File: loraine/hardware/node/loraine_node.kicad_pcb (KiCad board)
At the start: 2 copper layers, 50.8 x 53.3 mm, 41 parts, among them CON1 BARREL_JACK, IC1 ATTINY2313A-S, P1 POWER_THRU, P2 POWER, P3 SOLDER_PAD, P4 ICSP, P5 OUTPUTS, P6 BUS, P7 BUS_THRU, Q1 BD679, Q2 BD679, Q3 BD679, Q4 BD679, Q5 BD679, Q6 BD679, Q7 BD679, Q8 BD679, U1 UA7805CKCT, U2 SN65176BD, U3 TL4242, U4 TL4242, U5 TL4242, X1 16MHz

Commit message: Split boards
Removed LEDs and TL4242s and sense resistors from main node board and added 3x SIL3 connectors
Added 2nd board containing heatsunk LED mounting, TL4242, sense resistors.
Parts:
- removed D1: STAR_LED, heatsunk_star_led:heatsunk_star_led_board
- removed R1, R2, R3: 0.47R 0.25W, Resistors_SMD:Resistor_SMD0805_HandSoldering
- removed U3, U4, U5: TL4242, 8-son:8-SON
- added K1: CONN_3, Connect:SIL-3, F.Cu at (59.9, 127.5)
- added K2: CONN_3, Connect:SIL-3, F.Cu at (78.5, 132.3)
- added K3: CONN_3, Connect:SIL-3, F.Cu at (100.6, 129.8)

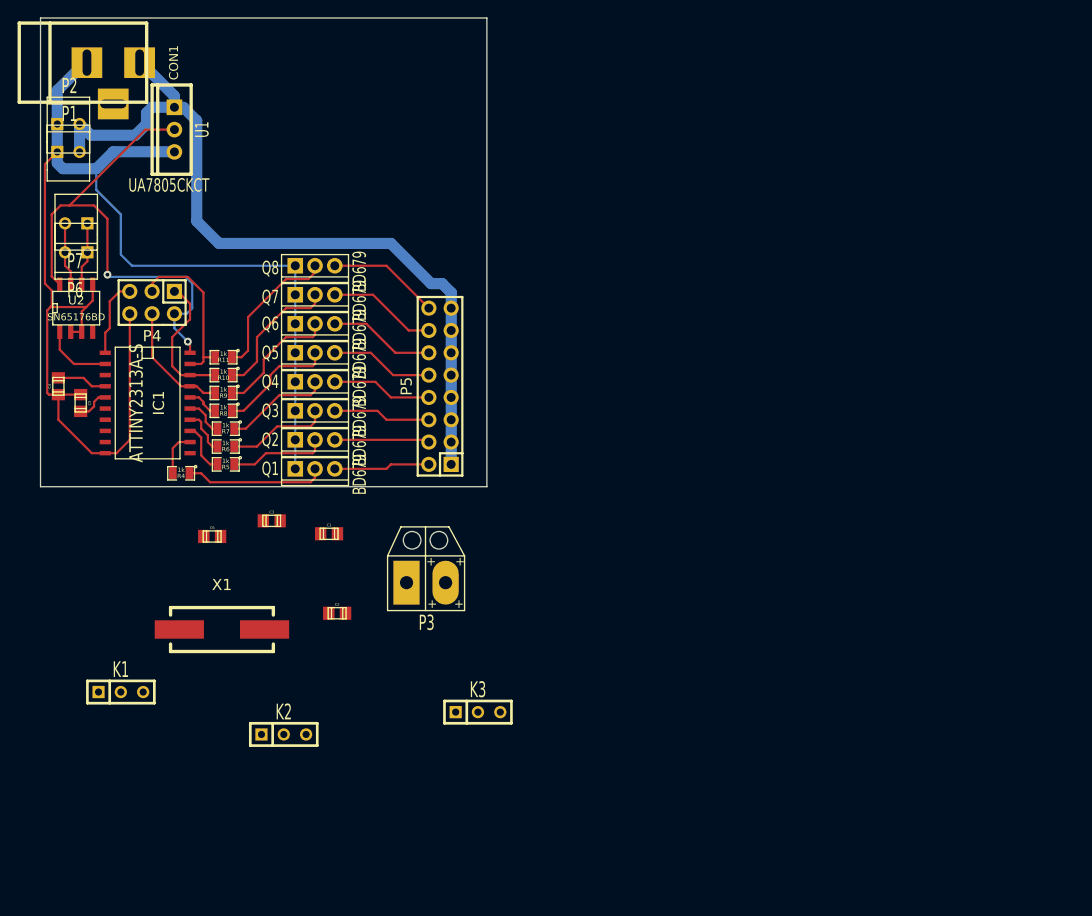
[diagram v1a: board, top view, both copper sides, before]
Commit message: Node PCB redo
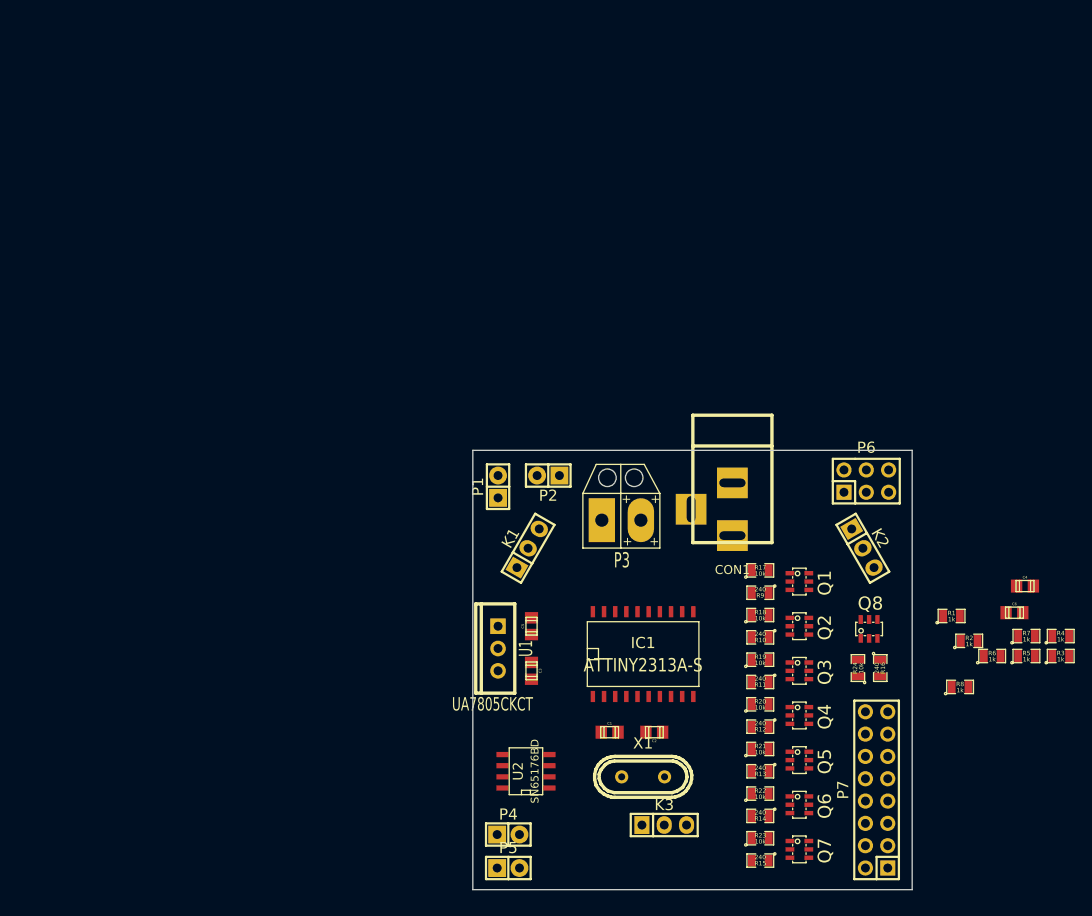
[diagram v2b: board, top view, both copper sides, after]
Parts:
- added R1: 1k, SMD_Packages:SM0805, F.Cu at (154.5, 118.9)
- added R12: 240, SMD_Packages:SM0805, F.Cu at (132.7, 131.4)
- added R13: 240, SMD_Packages:SM0805, F.Cu at (132.7, 136.5)
- added R14: 240, SMD_Packages:SM0805, F.Cu at (132.7, 141.6)
- added R15: 240, SMD_Packages:SM0805, F.Cu at (132.7, 146.7)
- added R16: 240, SMD_Packages:SM0805, F.Cu at (146.4, 124.8)
- added R17: 10k, SMD_Packages:SM0805, F.Cu at (132.7, 113.7)
- added R18: 10k, SMD_Packages:SM0805, F.Cu at (132.7, 118.7)
- added R19: 10k, SMD_Packages:SM0805, F.Cu at (132.7, 123.8)
- added R2: 1k, SMD_Packages:SM0805, F.Cu at (156.5, 121.7)
- added R20: 10k, SMD_Packages:SM0805, F.Cu at (132.7, 128.9)
- added R21: 10k, SMD_Packages:SM0805, F.Cu at (132.7, 134.0)
- added R22: 10k, SMD_Packages:SM0805, F.Cu at (132.7, 139.1)
- added R23: 10k, SMD_Packages:SM0805, F.Cu at (132.7, 144.1)
- added R24: 10k, SMD_Packages:SM0805, F.Cu at (143.8, 124.8)
- added R3: 1k, SMD_Packages:SM0805, F.Cu at (166.9, 123.4)
- C1: value 0.33uF -> 16pF
- C2: value 0.1uF -> 16pF
- C3: value 0.1uF -> 0.33uF
- C4, C5: value 16pF -> 0.1uF
- K1: value CONN_3 -> LED1; footprint Connect:SIL-3 -> Pin_Headers:Pin_Header_Straight_1x03
- K2: value CONN_3 -> LED2; footprint Connect:SIL-3 -> Pin_Headers:Pin_Header_Straight_1x03
- K3: value CONN_3 -> LED3; footprint Connect:SIL-3 -> Pin_Headers:Pin_Header_Straight_1x03
- P1, P2: footprint molex-22-23-2021:SIL-2 -> Pin_Headers:Pin_Header_Straight_1x02
- P4: value ICSP -> BUS; footprint Pin_Headers:Pin_Header_Straight_2x03 -> Pin_Headers:Pin_Header_Straight_1x02
- P5: value OUTPUTS -> BUS_THRU; footprint Pin_Headers:Pin_Header_Straight_2x08 -> Pin_Headers:Pin_Header_Straight_1x02
- P6: value BUS -> ICSP; footprint molex-22-23-2021:SIL-2 -> Pin_Headers:Pin_Header_Straight_2x03
- P7: value BUS_THRU -> OUTPUTS; footprint molex-22-23-2021:SIL-2 -> Pin_Headers:Pin_Header_Straight_2x08
- Q1, Q2, Q3, Q4, Q5, Q6, Q7, Q8: value BD679 -> TSM3460CX6; footprint to126:TO126 -> sot26:sot26
- R10, R11, R9: value 1k -> 240
- U2: footprint SOIC_Packages:SOIC-8_N -> SMD_Packages:SO8E
- X1: footprint Crystals:Crystal_HC49-SD_SMD -> Crystals:Crystal_HC49-U_Vertical
- moved C4 112.3 mm to (162.8, 115.4), turned to 0 degrees
- moved P7 111.6 mm to (145.9, 138.6), turned to 90 degrees
- moved R4 101.8 mm to (166.9, 121.1), turned to 0 degrees
- moved R7 94.1 mm to (163.0, 121.1), turned to 0 degrees
- moved R5 93.7 mm to (163.0, 123.4), turned to 0 degrees
- moved P6 93.6 mm to (144.8, 103.5), turned to 0 degrees
- moved C6 91.7 mm to (161.6, 118.5)
- moved R6 90.4 mm to (159.1, 123.4), turned to 0 degrees
- moved R8 89.5 mm to (155.5, 126.9), turned to 0 degrees
- moved CON1 87.7 mm to (129.5, 103.5), turned to 270 degrees
- moved Q7 83.8 mm to (137.2, 145.4)
- moved Q6 77.7 mm to (137.2, 140.3)
- moved Q8 75.4 mm to (145.1, 120.3), turned to 0 degrees
- moved U2 73.5 mm to (106.0, 136.5), turned to 90 degrees
- moved P4 72.9 mm to (104.0, 143.7), turned to 0 degrees
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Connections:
- C1 pad 1: +12V -> Net-(C1-Pad1)
- C2 pad 1: VCC -> Net-(C2-Pad1)
- C3 pad 1: GND -> +12V
- C3 pad 2: VCC -> GND
- C4 pad 1: Net-(C4-Pad1) -> GND
- C4 pad 2: GND -> +5V
- C5 pad 1: Net-(C5-Pad1) -> +5V
- C6 pad 2: VCC -> +5V
- CON1 pad 3: Net-(CON1-Pad3) -> (no net)
- IC1 pad 11: Net-(IC1-Pad11) -> (no net)
- IC1 pad 20: VCC -> +5V
- IC1 pad 3: Net-(IC1-Pad3) -> (no net)
- IC1 pad 4: Net-(C4-Pad1) -> Net-(C1-Pad1)
- IC1 pad 5: Net-(C5-Pad1) -> Net-(C2-Pad1)
- IC1 pad 6: Net-(IC1-Pad6) -> (no net)
- IC1 pad 7: Net-(IC1-Pad7) -> (no net)
- IC1 pad 8: Net-(IC1-Pad8) -> (no net)
- IC1 pad 9: Net-(IC1-Pad9) -> (no net)
- P4 pad 1: /MISO -> Net-(P4-Pad1)
- P4 pad 2: VCC -> Net-(P4-Pad2)
- P5 pad 1: +12V -> Net-(P4-Pad1)
- P5 pad 2: Net-(P5-Pad2) -> Net-(P4-Pad2)
- P6 pad 1: Net-(P6-Pad1) -> /MISO
- P6 pad 2: Net-(P6-Pad2) -> +5V
- P7 pad 1: Net-(P6-Pad1) -> +12V
- P7 pad 2: Net-(P6-Pad2) -> Net-(P7-Pad2)
- R10 pad 1: Net-(Q7-Pad3) -> Net-(Q2-PadG)
- R10 pad 2: /MISO -> Net-(R10-Pad2)
- R11 pad 1: Net-(Q8-Pad3) -> Net-(Q3-PadG)
- R11 pad 2: /SCK -> Net-(R11-Pad2)
- R4 pad 1: Net-(Q1-Pad3) -> Net-(R12-Pad2)
- R4 pad 2: Net-(IC1-Pad12) -> Net-(IC1-Pad15)
- R5 pad 1: Net-(Q2-Pad3) -> Net-(R13-Pad2)
- R5 pad 2: Net-(IC1-Pad13) -> Net-(IC1-Pad16)
- R6 pad 1: Net-(Q3-Pad3) -> Net-(R14-Pad2)
- R6 pad 2: Net-(IC1-Pad14) -> /MOSI
- R7 pad 1: Net-(Q4-Pad3) -> Net-(R15-Pad2)
- R7 pad 2: Net-(IC1-Pad15) -> /MISO
- R8 pad 1: Net-(Q5-Pad3) -> Net-(R16-Pad2)
- R8 pad 2: Net-(IC1-Pad16) -> /SCK
- R9 pad 1: Net-(Q6-Pad3) -> Net-(Q1-PadG)
- R9 pad 2: /MOSI -> Net-(R1-Pad1)
- U1 pad 1: +12V -> +5V
- U1 pad 2: GND -> +12V
- U1 pad 3: VCC -> GND
- U2 pad 4: Net-(U2-Pad4) -> (no net)
- U2 pad 6: Net-(P6-Pad1) -> Net-(P4-Pad1)
- U2 pad 7: Net-(P6-Pad2) -> Net-(P4-Pad2)
- U2 pad 8: VCC -> +5V
- X1 pad 1: Net-(C4-Pad1) -> Net-(C1-Pad1)
- X1 pad 2: Net-(C5-Pad1) -> Net-(C2-Pad1)
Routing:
- net GND: track 153.3 -> 0.00 mm
- net +12V: track 89.8 -> 0.00 mm
- net VCC: track 58.0 -> 0.00 mm, vias 2 -> 0
- net /SCK: track 18.6 -> 0.00 mm
- net Net-(Q8-Pad3): track 16.5 -> 0.00 mm
- net Net-(Q1-Pad3): track 15.9 -> 0.00 mm
- net /MISO: track 15.6 -> 0.00 mm
- net Net-(Q7-Pad3): track 15.5 -> 0.00 mm
- net Net-(Q6-Pad3): track 14.4 -> 0.00 mm
- net /MOSI: track 13.8 -> 0.00 mm
- net Net-(Q5-Pad3): track 13.5 -> 0.00 mm
- net Net-(P5-Pad16): track 12.7 -> 0.00 mm
- net Net-(P5-Pad14): track 12.4 -> 0.00 mm
- net Net-(P5-Pad12): track 12.1 -> 0.00 mm
- net Net-(Q4-Pad3): track 12.0 -> 0.00 mm
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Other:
- board size 50.8 x 53.3 mm -> 50 x 50 mm
- net class chunky removed
- net class signal removed

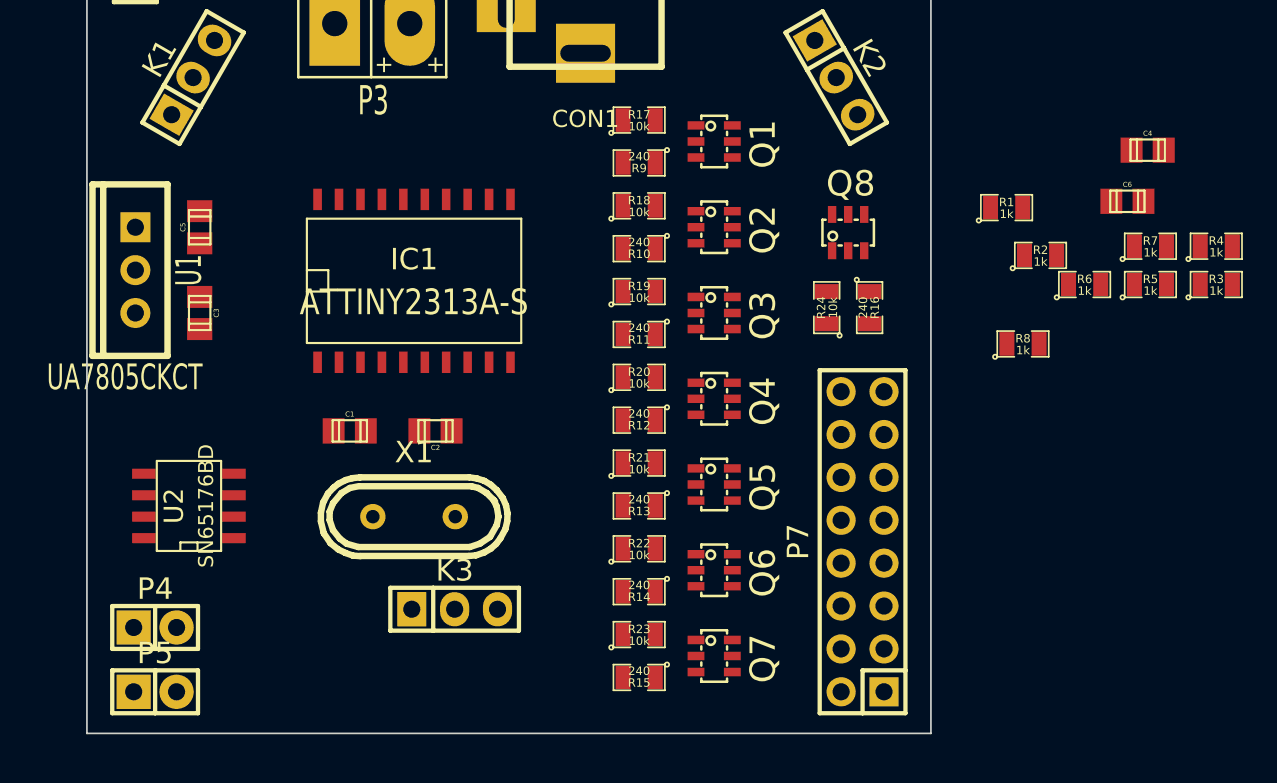
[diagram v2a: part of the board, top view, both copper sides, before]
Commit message: Finished footprint placement on node board
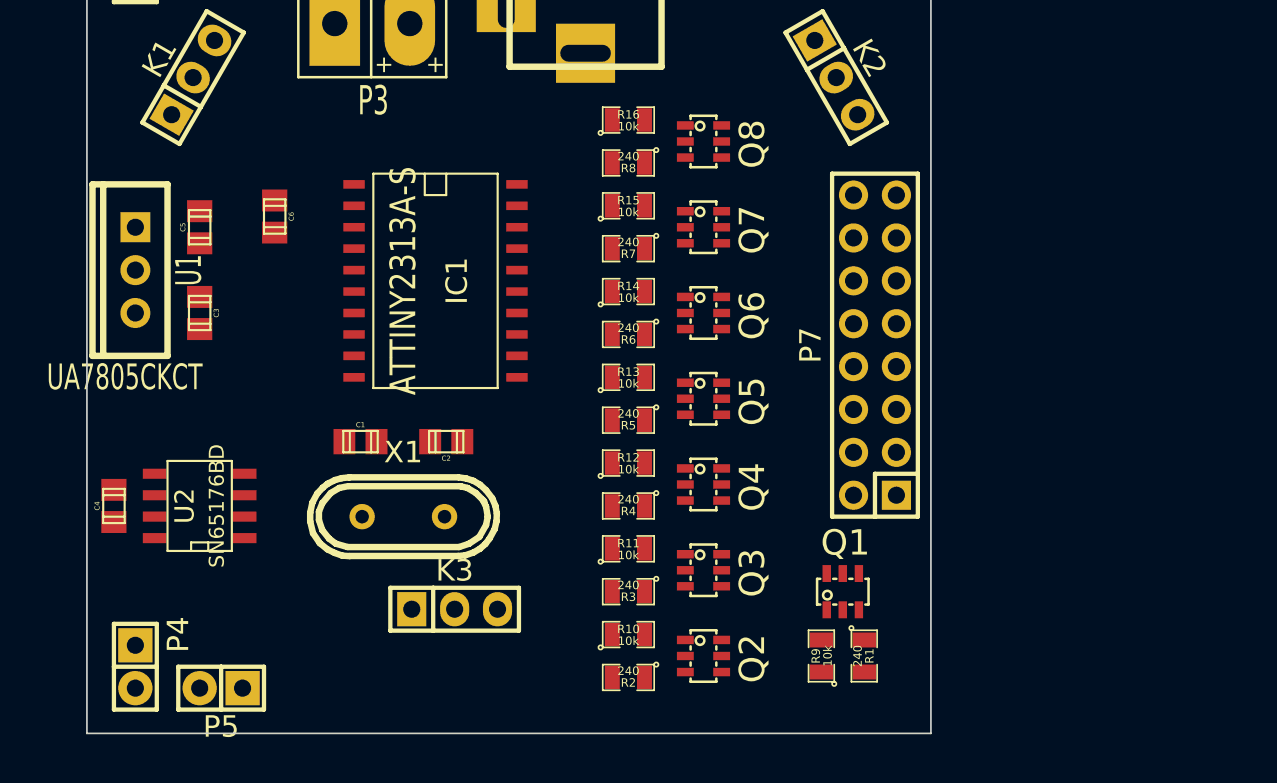
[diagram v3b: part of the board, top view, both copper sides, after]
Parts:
- removed the R1 at (154.5, 118.9)
- removed the R16 at (146.4, 124.8)
- removed R18: 10k, SMD_Packages:SM0805
- removed the R3 at (166.9, 123.4)
- removed the R4 at (166.9, 121.1)
- removed the R5 at (163.0, 123.4)
- removed the R6 at (159.1, 123.4)
- removed the R7 at (163.0, 121.1)
- R10: value 240 -> 10k
- R2, R8: value 1k -> 240
- moved C4 64.8 mm to (101.6, 136.5), turned to 90 degrees
- moved C6 50.5 mm to (111.1, 119.4), turned to 270 degrees
- moved R2 34.9 mm to (132.1, 146.7), turned to 180 degrees
- moved R9 33.5 mm to (143.5, 145.4), turned to 90 degrees
- moved R1 32.1 mm to (146.1, 145.4), turned to 270 degrees
- moved Q1 27.7 mm to (144.8, 141.6), turned to 0 degrees
- moved R8 25.7 mm to (132.1, 116.2), turned to 180 degrees
- moved R15 25.4 mm to (132.1, 118.7)
- moved R7 25.4 mm to (132.1, 121.3)
- moved Q2 25.4 mm to (136.5, 145.4)
- moved Q7 25.4 mm to (136.5, 120.0)
- moved R10 22.9 mm to (132.1, 144.1), turned to 0 degrees
- moved R16 16.2 mm to (132.1, 113.7), turned to 0 degrees
- moved Q3 15.3 mm to (136.5, 140.3)
- moved Q6 15.3 mm to (136.5, 125.1)
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- renumbered R9 to R1, R19 to R11, R20 to R12, R21 to R13, R22 to R14, R23 to R15, R24 to R16, R11 to R3, R12 to R4, R13 to R5, R14 to R6, R15 to R7, R17 to R9
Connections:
- K1 pad 2: Net-(IC1-Pad12) -> Net-(IC1-Pad14)
- K3 pad 2: Net-(IC1-Pad14) -> Net-(IC1-Pad12)
- R1 pad 2: Net-(R1-Pad1) -> Net-(IC1-Pad12)
- R10 pad 1: Net-(Q2-PadG) -> GND
- R10 pad 2: Net-(R10-Pad2) -> Net-(Q2-PadG)
- R2 pad 1: Net-(R10-Pad2) -> Net-(Q2-PadG)
- R3 pad 2: Net-(R11-Pad2) -> Net-(IC1-Pad14)
- R4 pad 2: Net-(R12-Pad2) -> Net-(IC1-Pad15)
- R5 pad 2: Net-(R13-Pad2) -> Net-(IC1-Pad16)
- R6 pad 2: Net-(R14-Pad2) -> /MOSI
- R7 pad 2: Net-(R15-Pad2) -> /MISO
- R8 pad 1: Net-(R16-Pad2) -> Net-(Q8-PadG)

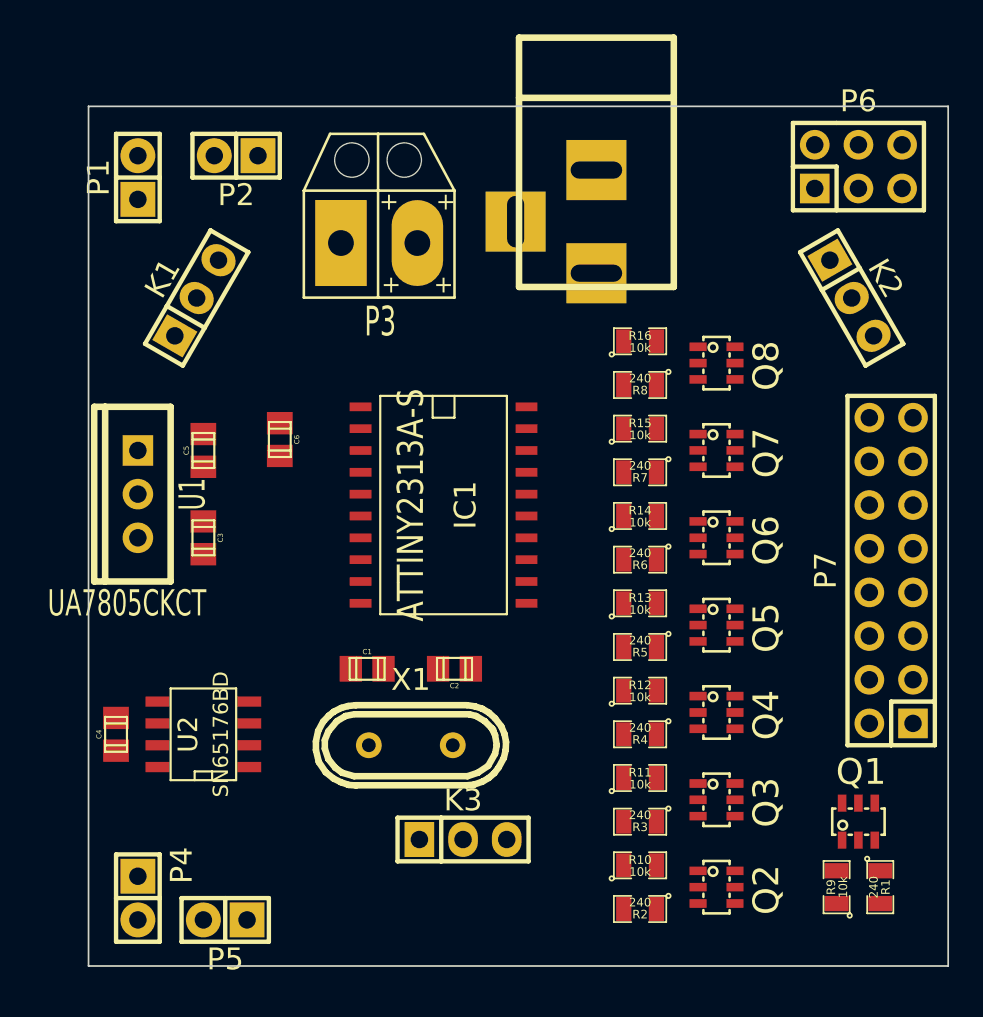
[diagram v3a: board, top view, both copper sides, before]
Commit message: Cleared up node pcb silk
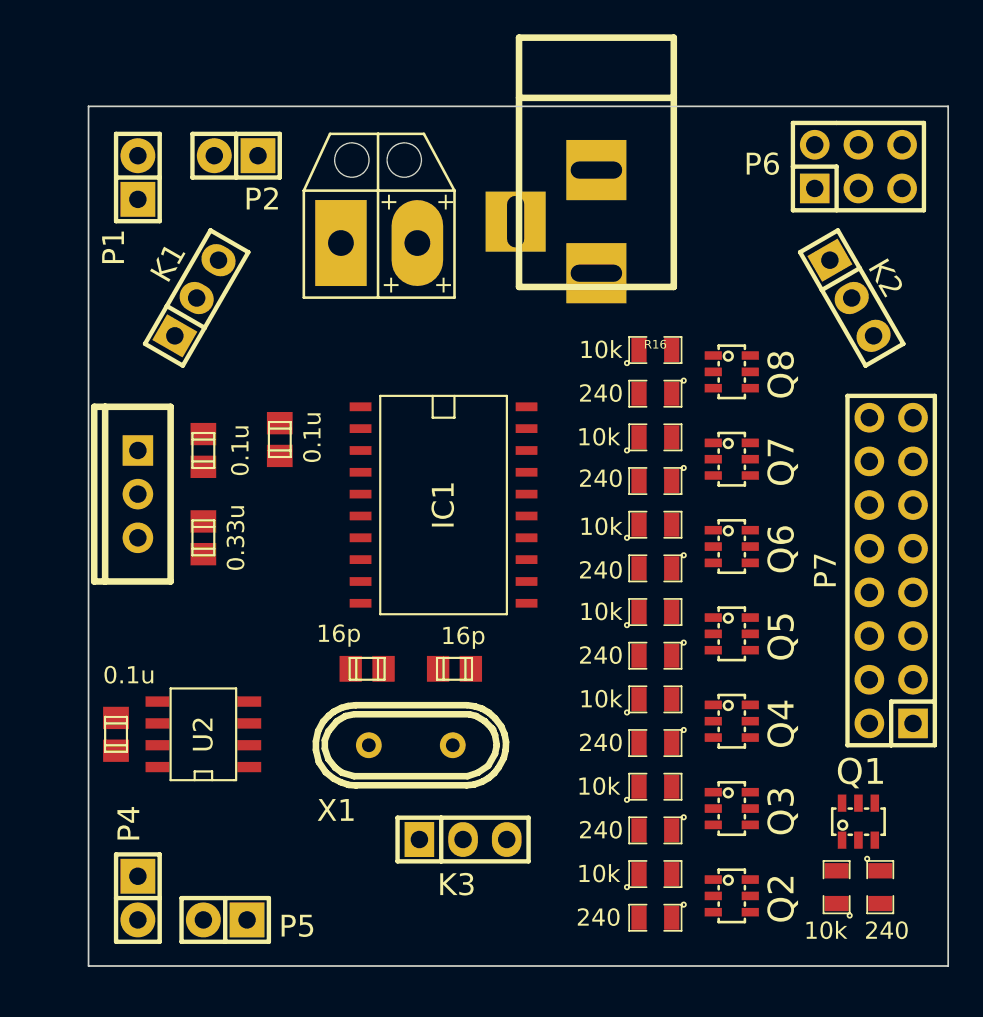
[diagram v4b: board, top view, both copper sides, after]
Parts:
- C1, C2: value 16pF -> 16p
- C3: value 0.33uF -> 0.33u
- C4, C5, C6: value 0.1uF -> 0.1u
- moved Q2 1.02 mm to (137.4, 145.9)
- moved Q4 1.02 mm to (137.4, 135.8)
- moved R11 1.02 mm to (133.0, 139.6)
- moved R13 1.02 mm to (133.0, 129.4)
- moved R2 1.02 mm to (133.0, 147.2)
- moved R3 1.02 mm to (133.0, 142.1)
- moved R5 1.02 mm to (133.0, 132.0)
- moved R6 1.02 mm to (133.0, 126.9)
- moved R7 1.02 mm to (133.0, 121.8)
- moved Q6 1.02 mm to (137.4, 125.6)
- moved Q7 1.02 mm to (137.4, 120.5)
- moved Q8 1.02 mm to (137.4, 115.4)
- moved R14 1.02 mm to (133.0, 124.3)
- moved R15 1.02 mm to (133.0, 119.3)
- moved R16 1.02 mm to (133.0, 114.2)
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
